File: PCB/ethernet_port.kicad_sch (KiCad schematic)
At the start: 62 parts, among them IC10 MMBT3904-AQ, IC11 MMBT3904-AQ, IC5 W5500, IC6 CP2102N-A02-GQFN24, IC7 USBLC6-2SC6, J1 USB_C_Receptacle_USB2.0_16P, J2 TMJ0026ABNL, Y3 ASE-25.000MHZ-LC-T

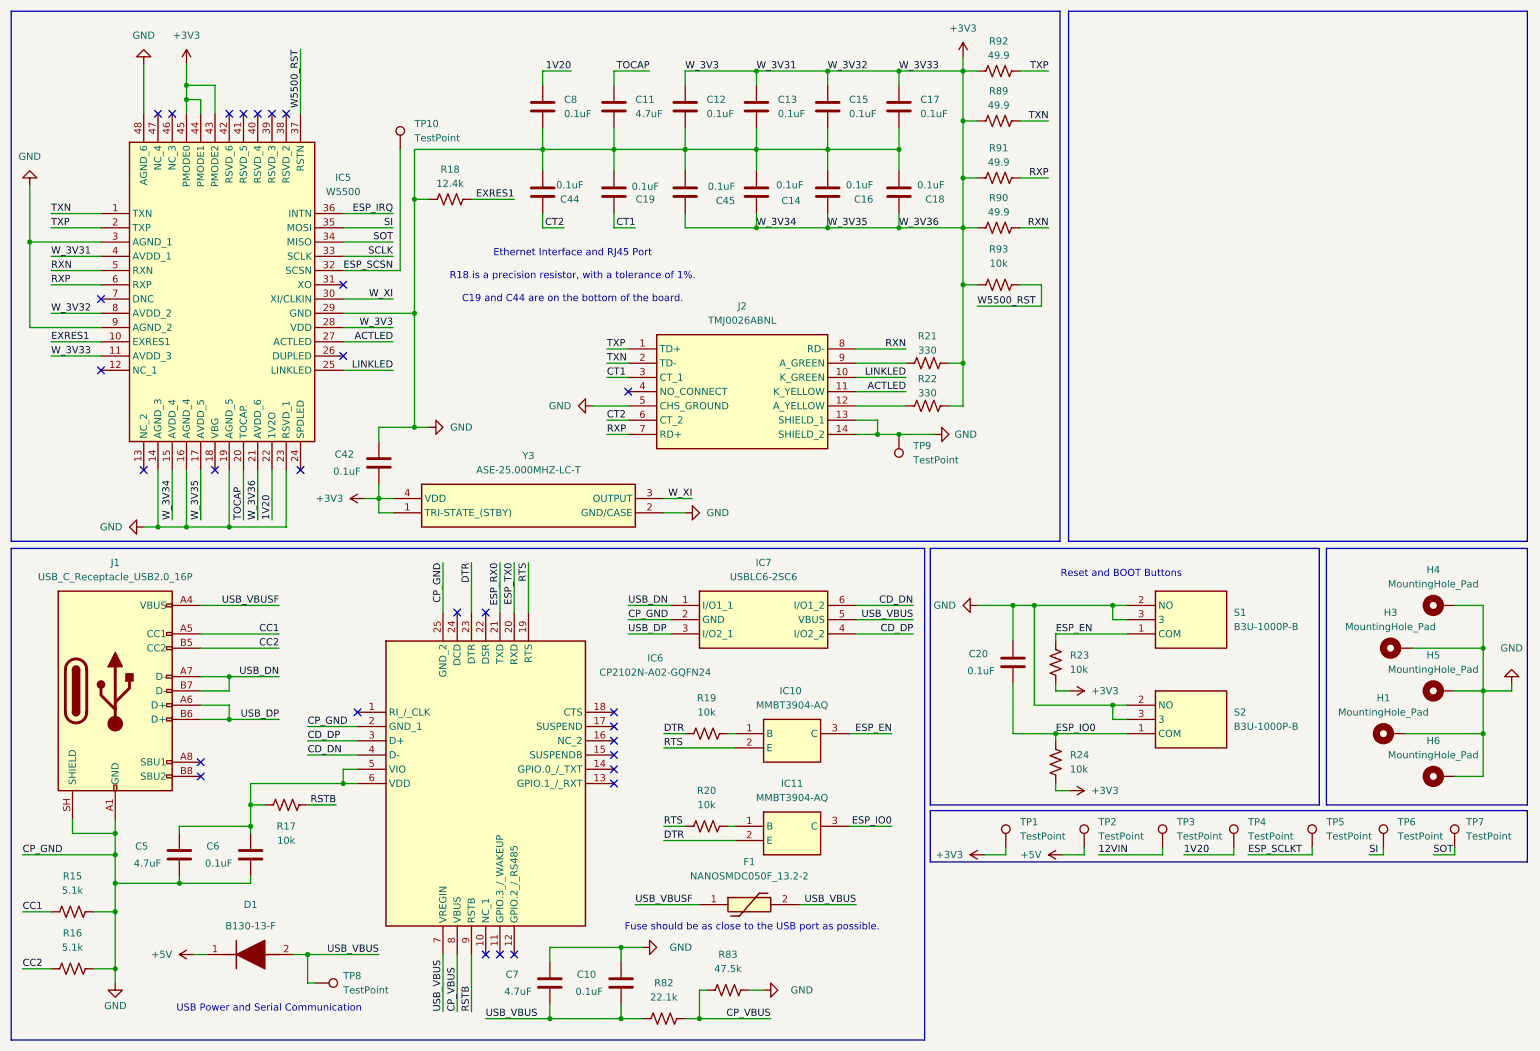
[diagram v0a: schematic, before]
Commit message: Updated PDF schematic, tweaked connections
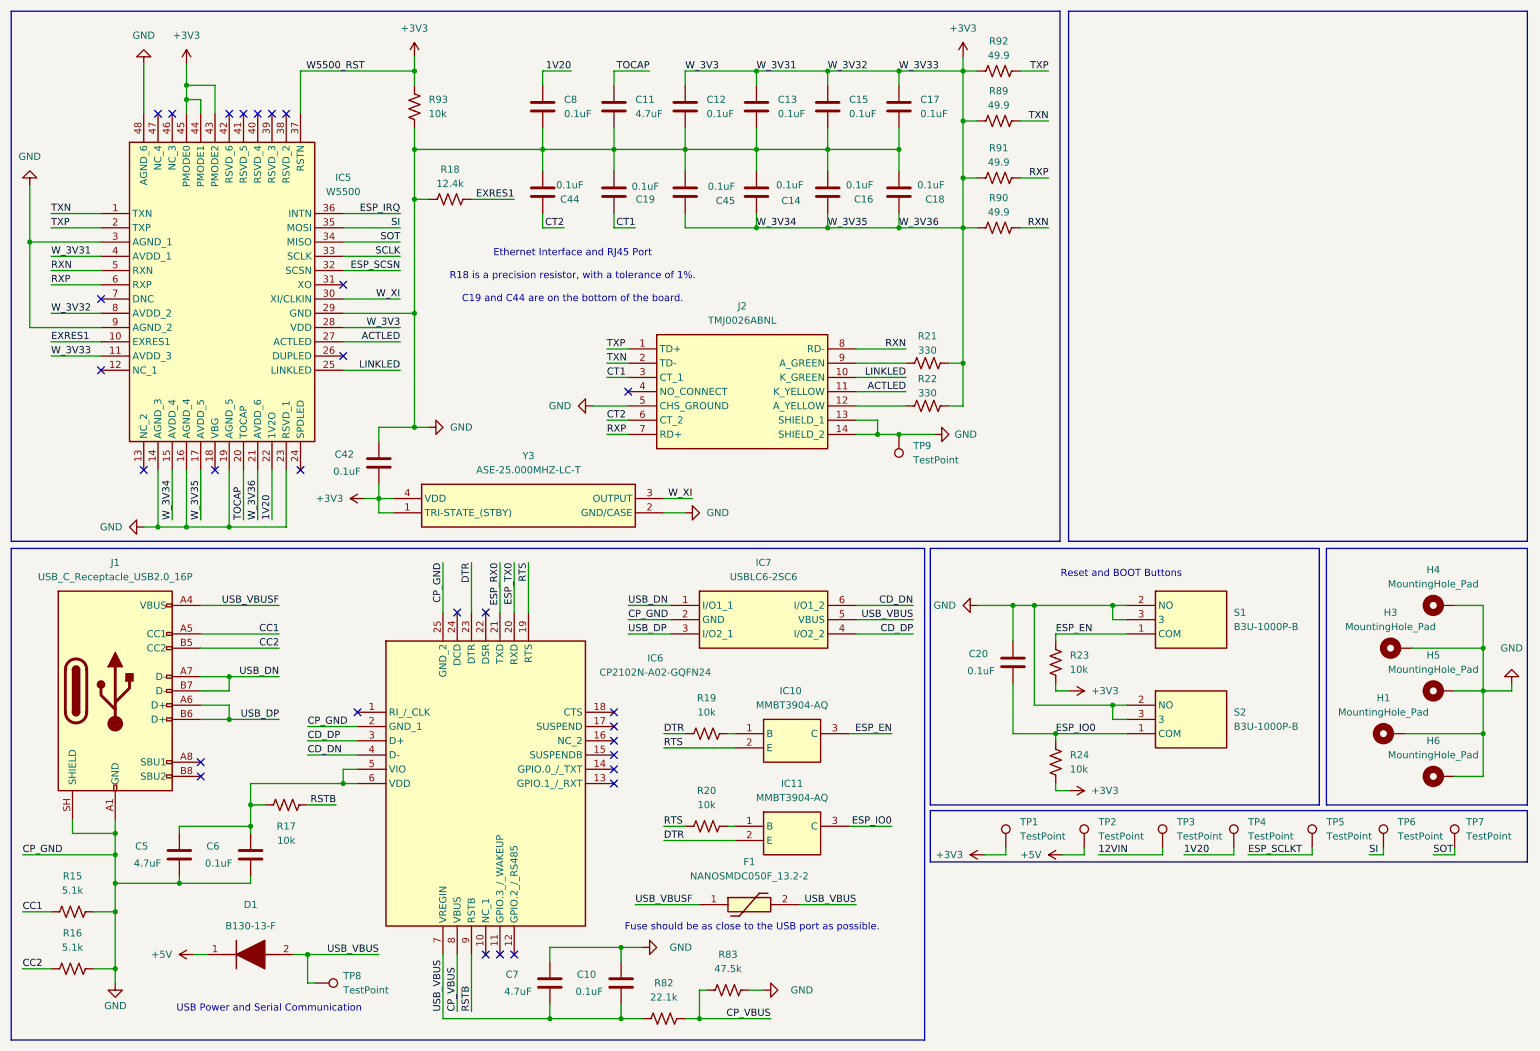
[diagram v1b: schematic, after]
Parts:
- removed TP10: TestPoint, TestPoint:TestPoint_Pad_D3.0mm, symbol Connector:TestPoint
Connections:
- net W5500_RST is gone; now on net +3V3: IC5.37 (RSTN), R93.2
- net +3V3: no longer R93.1
- net GND: now also R93.1
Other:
- moved on the sheet: R93

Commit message: Touch-ups
Various minor improvements
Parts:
- removed R93: 10k, Resistor_SMD:R_0805_2012Metric_Pad1.20x1.40mm_HandSolder, symbol Device:R_US
- added R94: 4.7k, Resistor_SMD:R_0805_2012Metric_Pad1.20x1.40mm_HandSolder, symbol Device:R_US
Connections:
- net +3V3: no longer IC5.37 (RSTN)
- new net: IC5.37 (RSTN), R94.2
- new net W5500_RST: R94.1
